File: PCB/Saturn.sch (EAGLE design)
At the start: 21 parts, among them U1A SN74AHCT125N, U2A SN74AHCT125N, U3A SN74AHCT125N, U4A SN74AHCT125N

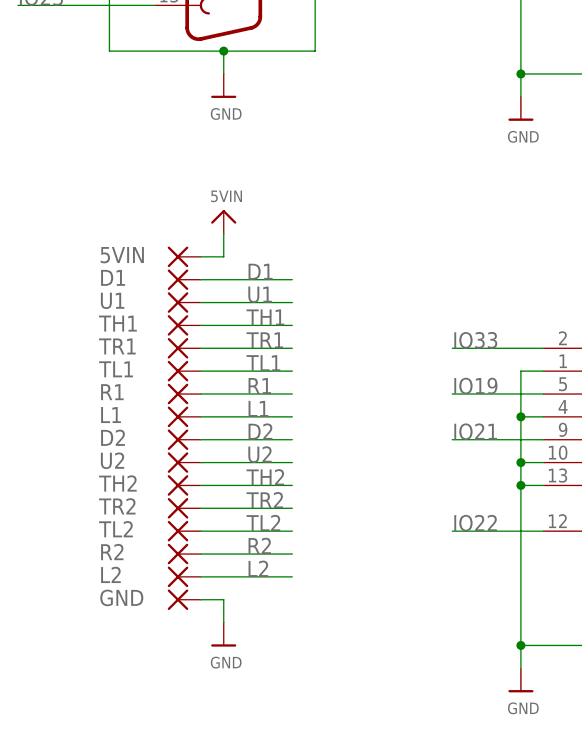
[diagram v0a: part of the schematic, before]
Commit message: Datasheets, BOM Update, 3 New PCBs
Added Datasheets for the Female/Male DB25 connectors
Updated formatting on the BOM

New PCBs:
Added Nintendo 64 (Updated to 1.1, Moved VIN from 5V to 3V3)
Added Sega Saturn (Updated to 1.1, Added 5V and GND Pads on bottom for Second player pads to ease install)
Added NES

Removed PSX/PS2 and Virtual Boy as work is not complete (New branches will be made for each one)
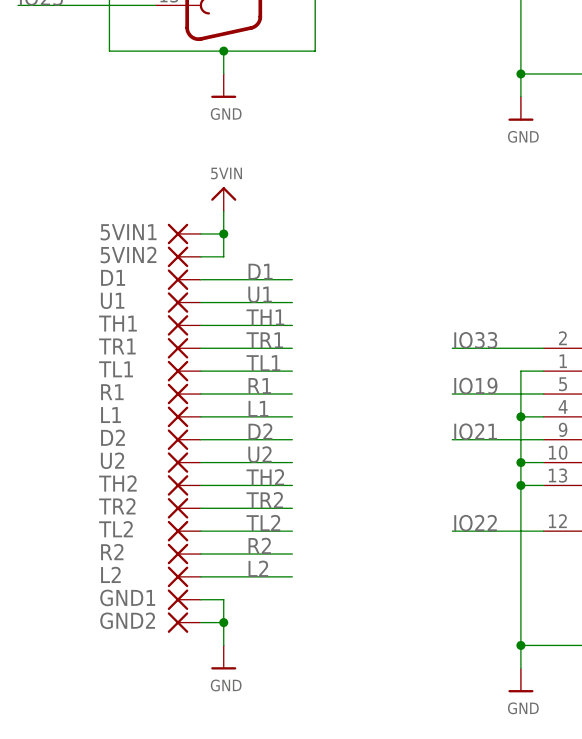
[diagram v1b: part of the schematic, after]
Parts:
- added 5VIN1, GND2: (no value), wirepad:SMD5
- renumbered 5VIN to 5VIN2, GND to GND1
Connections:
- net 5VIN: now also 5VIN1.P
- net GND: now also GND2.P
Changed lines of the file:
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@@
 <part name="U$49" library="microbuilder" deviceset="VIN" device="" value="3v3in"/>
 <part name="U$11" library="microbuilder" deviceset="VIN" device="" value="5VIN"/>
-<part name="5VIN" library="wirepad" library_urn="urn:adsk.eagle:library:412" deviceset="SMD5" device="" package3d_urn="urn:adsk.eagle:package:30841/1"/>
+<part name="5VIN1" library="wirepad" library_urn="urn:adsk.eagle:library:412" deviceset="SMD5" device="" package3d_urn="urn:adsk.eagle:package:30841/1"/>
 <part name="R1" library="wirepad" library_urn="urn:adsk.eagle:library:412" deviceset="SMD5" device="" package3d_urn="urn:adsk.eagle:package:30841/1"/>
 <part name="TL1" library="wirepad" library_urn="urn:adsk.eagle:library:412" deviceset="SMD5" device="" package3d_urn="urn:adsk.eagle:package:30841/1"/>
@@
 <part name="TH2" library="wirepad" library_urn="urn:adsk.eagle:library:412" deviceset="SMD5" device="" package3d_urn="urn:adsk.eagle:package:30841/1"/>
 <part name="U2" library="wirepad" library_urn="urn:adsk.eagle:library:412" deviceset="SMD5" device="" package3d_urn="urn:adsk.eagle:package:30841/1"/>
-<part name="GND" library="wirepad" library_urn="urn:adsk.eagle:library:412" deviceset="SMD5" device="" package3d_urn="urn:adsk.eagle:package:30841/1"/>
+<part name="GND1" library="wirepad" library_urn="urn:adsk.eagle:library:412" deviceset="SMD5" device="" package3d_urn="urn:adsk.eagle:package:30841/1"/>
+<part name="5VIN2" library="wirepad" library_urn="urn:adsk.eagle:library:412" deviceset="SMD5" device="" package3d_urn="urn:adsk.eagle:package:30841/1"/>
+<part name="GND2" library="wirepad" library_urn="urn:adsk.eagle:library:412" deviceset="SMD5" device="" package3d_urn="urn:adsk.eagle:package:30841/1"/>
 </parts>
 <sheets>
@@
 <attribute name="VALUE" x="310.896" y="-65.024" size="1.27" layer="96"/>
 </instance>
-<instance part="U$11" gate="G$1" x="238.76" y="-127" smashed="yes">
-<attribute name="VALUE" x="237.236" y="-125.984" size="1.27" layer="96"/>
-</instance>
-<instance part="5VIN" gate="1" x="233.68" y="-132.08" smashed="yes">
-<attribute name="NAME" x="224.917" y="-132.7658" size="1.778" layer="95"/>
-<attribute name="VALUE" x="232.537" y="-135.382" size="1.778" layer="96"/>
+<instance part="U$11" gate="G$1" x="238.76" y="-124.46" smashed="yes">
+<attribute name="VALUE" x="237.236" y="-123.444" size="1.27" layer="96"/>
+</instance>
+<instance part="5VIN1" gate="1" x="233.68" y="-129.54" smashed="yes">
+<attribute name="NAME" x="224.917" y="-130.2258" size="1.778" layer="95"/>
+<attribute name="VALUE" x="232.537" y="-132.842" size="1.778" layer="96"/>
 </instance>
 <instance part="R1" gate="1" x="233.68" y="-147.32" smashed="yes">
@@
 <attribute name="VALUE" x="394.716" y="-62.484" size="1.27" layer="96"/>
 </instance>
-<instance part="U$5" gate="G$1" x="238.76" y="-175.26" smashed="yes">
-<attribute name="VALUE" x="237.236" y="-177.8" size="1.27" layer="96"/>
+<instance part="U$5" gate="G$1" x="238.76" y="-177.8" smashed="yes">
+<attribute name="VALUE" x="237.236" y="-180.34" size="1.27" layer="96"/>
 </instance>
 <instance part="D2" gate="1" x="233.68" y="-152.4" smashed="yes">
@@
 <attribute name="VALUE" x="232.537" y="-158.242" size="1.778" layer="96"/>
 </instance>
-<instance part="GND" gate="1" x="233.68" y="-170.18" smashed="yes">
+<instance part="GND1" gate="1" x="233.68" y="-170.18" smashed="yes">
 <attribute name="NAME" x="224.917" y="-170.8658" size="1.778" layer="95"/>
 <attribute name="VALUE" x="232.537" y="-173.482" size="1.778" layer="96"/>
+</instance>
+<instance part="5VIN2" gate="1" x="233.68" y="-132.08" smashed="yes">
+<attribute name="NAME" x="224.917" y="-132.7658" size="1.778" layer="95"/>
+<attribute name="VALUE" x="232.537" y="-135.382" size="1.778" layer="96"/>
+</instance>
+<instance part="GND2" gate="1" x="233.68" y="-172.72" smashed="yes">
+<attribute name="NAME" x="224.917" y="-173.4058" size="1.778" layer="95"/>
+<attribute name="VALUE" x="232.537" y="-176.022" size="1.778" layer="96"/>
 </instance>
 </instances>
@@
 </segment>
 <segment>
-<pinref part="GND" gate="1" pin="P"/>
+<pinref part="GND1" gate="1" pin="P"/>
 <wire x1="236.22" y1="-170.18" x2="238.76" y2="-170.18" width="0.1524" layer="91"/>
 <wire x1="238.76" y1="-170.18" x2="238.76" y2="-172.72" width="0.1524" layer="91"/>
 <pinref part="U$5" gate="G$1" pin="GND"/>
+<pinref part="GND2" gate="1" pin="P"/>
+<wire x1="238.76" y1="-172.72" x2="238.76" y2="-175.26" width="0.1524" layer="91"/>
+<wire x1="236.22" y1="-172.72" x2="238.76" y2="-172.72" width="0.1524" layer="91"/>
+<junction x="238.76" y="-172.72"/>
 </segment>
 </net>
@@
 </segment>
 <segment>
-<pinref part="5VIN" gate="1" pin="P"/>
+<pinref part="5VIN1" gate="1" pin="P"/>
+<wire x1="236.22" y1="-129.54" x2="238.76" y2="-129.54" width="0.1524" layer="91"/>
+<wire x1="238.76" y1="-129.54" x2="238.76" y2="-127" width="0.1524" layer="91"/>
+<pinref part="U$11" gate="G$1" pin="VIN"/>
+<pinref part="5VIN2" gate="1" pin="P"/>
 <wire x1="236.22" y1="-132.08" x2="238.76" y2="-132.08" width="0.1524" layer="91"/>
 <wire x1="238.76" y1="-132.08" x2="238.76" y2="-129.54" width="0.1524" layer="91"/>
-<pinref part="U$11" gate="G$1" pin="VIN"/>
-</segment>
-<segment>
+<junction x="238.76" y="-129.54"/>
+</segment>
+<segment>

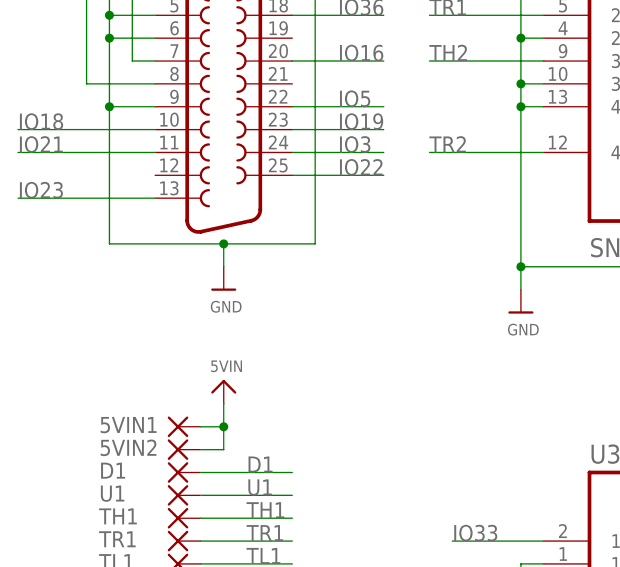
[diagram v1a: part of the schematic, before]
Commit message: Added exposed GND plane at DB25 anchors
All PCBs have been update to have exposed GND plane pads for the DB25 anchor points.

This resolves Issue 54
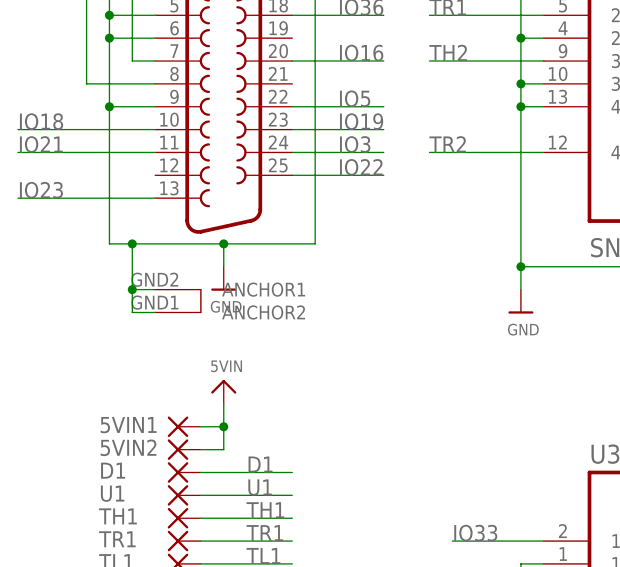
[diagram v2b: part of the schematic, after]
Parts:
- X1: device SparkFun-Retired:DB25_FEMALEH -> SparkFun-Retired:DB25_FEMALEHP
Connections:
- net GND: now also X1.ANCHOR1, X1.ANCHOR2
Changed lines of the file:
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@@
 </classes>
 <parts>
-<part name="X1" library="SparkFun-Retired" deviceset="DB25_FEMALE" device="H"/>
+<part name="X1" library="SparkFun-Retired" deviceset="DB25_FEMALE" device="HP"/>
 <part name="U$43" library="microbuilder" deviceset="VIN" device="" value="3V3IN"/>
 <part name="U$44" library="microbuilder" deviceset="VIN" device="" value="5VIN"/>
@@
 <wire x1="238.76" y1="-109.22" x2="238.76" y2="-111.76" width="0.1524" layer="91"/>
 <junction x="238.76" y="-109.22"/>
-<wire x1="238.76" y1="-109.22" x2="226.06" y2="-109.22" width="0.1524" layer="91"/>
+<wire x1="238.76" y1="-109.22" x2="228.6" y2="-109.22" width="0.1524" layer="91"/>
 <pinref part="X1" gate="-1" pin="3"/>
+<wire x1="228.6" y1="-109.22" x2="226.06" y2="-109.22" width="0.1524" layer="91"/>
 <wire x1="231.14" y1="-78.74" x2="226.06" y2="-78.74" width="0.1524" layer="91"/>
 <pinref part="X1" gate="-1" pin="6"/>
@@
 <wire x1="246.38" y1="-81.28" x2="248.92" y2="-81.28" width="0.1524" layer="91"/>
 <wire x1="248.92" y1="-81.28" x2="248.92" y2="-109.22" width="0.1524" layer="91"/>
+<wire x1="228.6" y1="-109.22" x2="228.6" y2="-114.3" width="0.1524" layer="91"/>
+<junction x="228.6" y="-109.22"/>
+<pinref part="X1" gate="-1" pin="ANCHOR2"/>
+<wire x1="228.6" y1="-114.3" x2="228.6" y2="-116.84" width="0.1524" layer="91"/>
+<wire x1="228.6" y1="-116.84" x2="231.14" y2="-116.84" width="0.1524" layer="91"/>
+<pinref part="X1" gate="-1" pin="ANCHOR1"/>
+<wire x1="228.6" y1="-114.3" x2="231.14" y2="-114.3" width="0.1524" layer="91"/>
+<junction x="228.6" y="-114.3"/>
 </segment>
 <segment>
